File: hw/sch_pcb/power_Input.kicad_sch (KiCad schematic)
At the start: 34 parts, among them J1 USBC_USB4105-GF-A, U1 USBLC6-2SC6

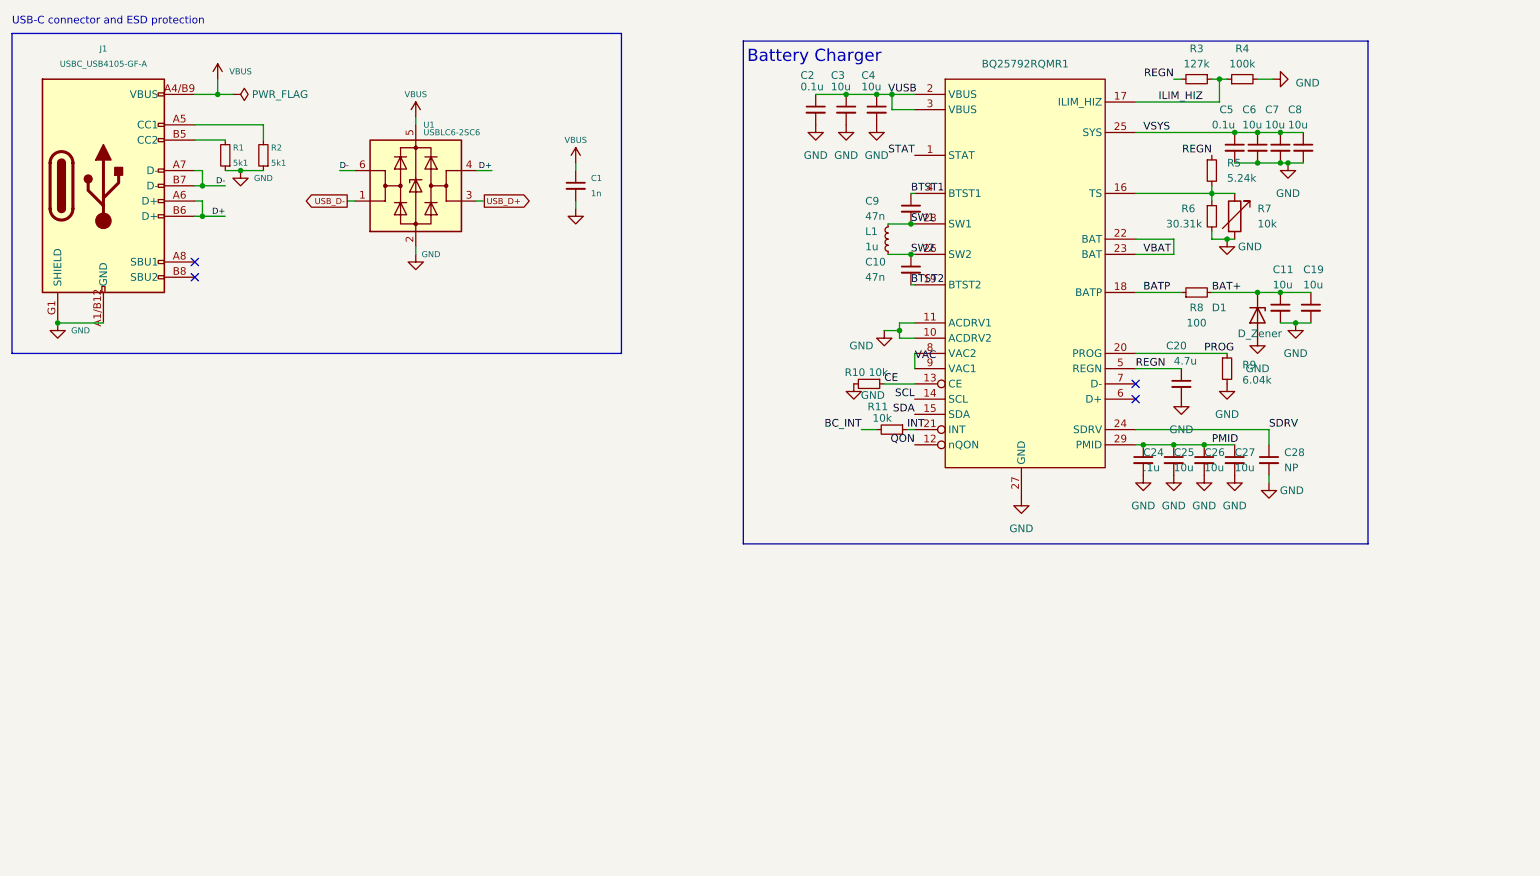
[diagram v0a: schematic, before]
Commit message: work of the schematics of charger completed.
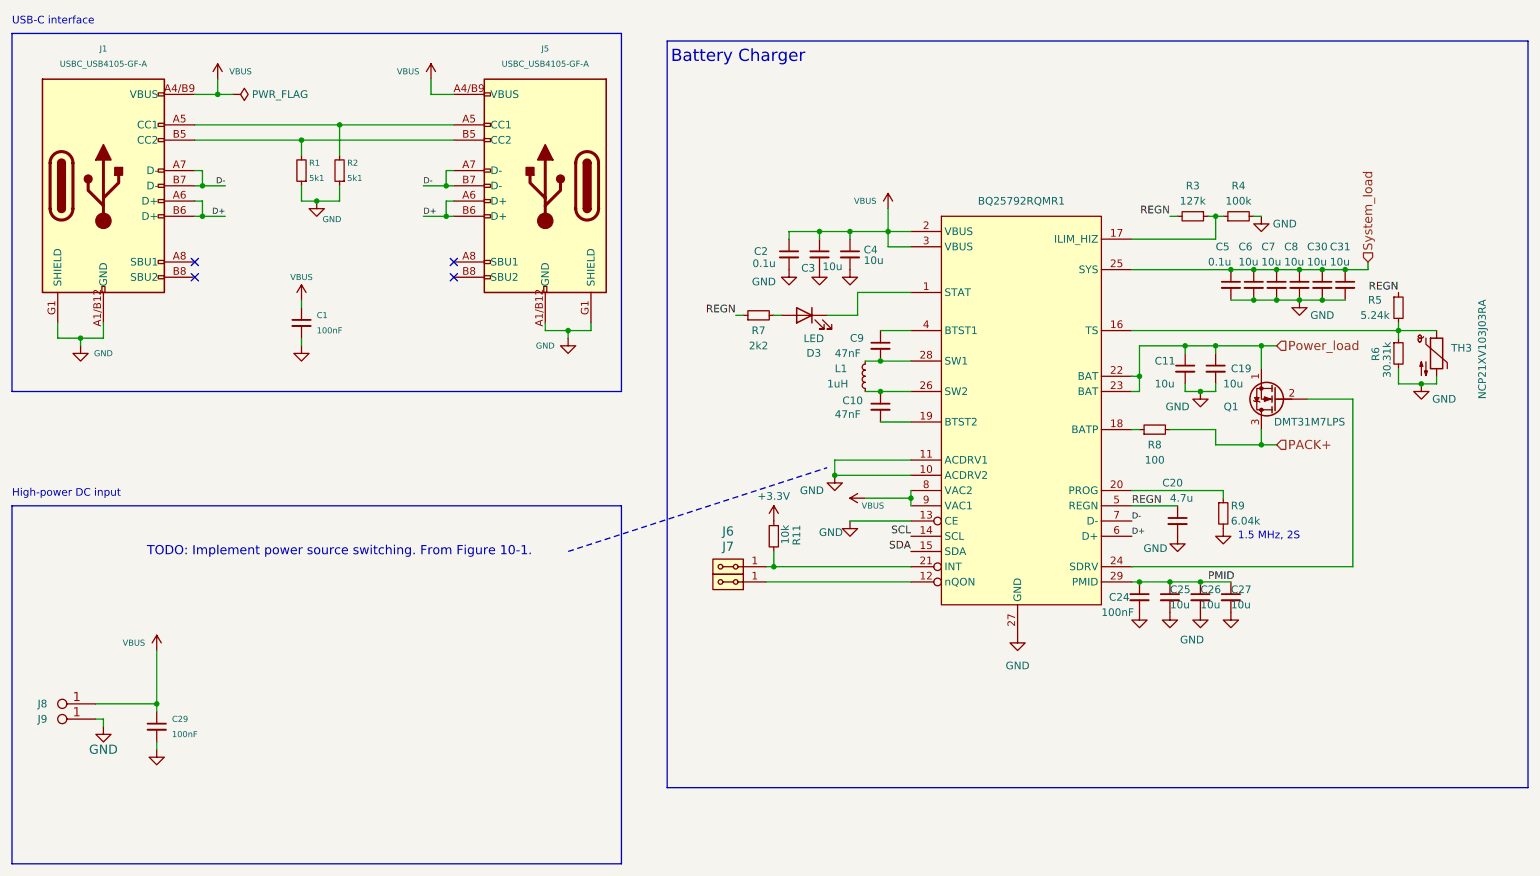
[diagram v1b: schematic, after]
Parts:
- removed C28: NP, Capacitor_SMD:C_0402_1005Metric, symbol Device:C_Small
- removed D1: D_Zener, Diode_SMD:D_SOD-323F, symbol Device:D_Zener
- removed R10: 10k, Resistor_SMD:R_0402_1005Metric, symbol Device:R_Small
- removed R7: 10k, Resistor_SMD:R_0402_1005Metric, symbol Device:R_Variable
- removed U1: USBLC6-2SC6, Package_TO_SOT_SMD:SOT-23-6, symbol Power_Protection:USBLC6-2SC6
- added C29: 100nF, Capacitor_SMD:C_0805_2012Metric, symbol Device:C_Small
- added C30, C31: 10u, Capacitor_SMD:C_0805_2012Metric, symbol Device:C_Small
- added D3: LED, symbol Device:LED
- added J5: USBC_USB4105-GF-A, Mlab_CON:USBC GCT_USB4105-GF-A, symbol MLAB_CONNECTORS:USBC_USB4105-GF-A
- added J6, J7: HEADER_2x01_PARALLEL, symbol MLAB_HEADER:HEADER_2x01_PARALLEL
- added J8, J9: CONN1_1, Mlab_Con:WAGO256, symbol LION2CELL01D-rescue:CONN1_1
- added Q1: DMT31M7LPS, Mlab_IO:PowerDI5060-8, symbol Device:Q_NMOS_SGD
- added R7: 2k2, Resistor_SMD:R_0805_2012Metric, symbol Device:R_Small
- added TH3: NCP21XV103J03RA, Resistor_SMD:R_0805_2012Metric, symbol Device:Thermistor_NTC
- C1: value 1n -> 100nF
- C10: value 47n -> 47nF; footprint Capacitor_SMD:C_0402_1005Metric -> Capacitor_SMD:C_0805_2012Metric
- C24: value .1u -> 100nF
- C9: value 47n -> 47nF
- L1: value 1u -> 1uH
- R8: footprint Resistor_SMD:R_0402_1005Metric -> Resistor_SMD:R_0805_2012Metric
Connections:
- net CE is gone; now on net GND: BQ25792RQMR1.13 (CE)
- net VAC is gone; now on net VBUS: BQ25792RQMR1.8 (VAC2), BQ25792RQMR1.9 (VAC1)
- net VBAT is gone; now on net Power_load: BQ25792RQMR1.22 (BAT), BQ25792RQMR1.23 (BAT)
- net VUSB is gone; now on net VBUS: BQ25792RQMR1.2 (VBUS), BQ25792RQMR1.3 (VBUS), C2.1, C3.1, C4.1
- net D+: now also BQ25792RQMR1.6 (D+), J5.A6 (D+), J5.B6 (D+)
- net D-: now also BQ25792RQMR1.7 (D-), J5.A7 (D-), J5.B7 (D-)
- net GND: now also C29.2, C30.2, C31.2, J5.A1/B12 (GND), J5.B1/A12 (GND), J5.G1 (SHIELD), J5.G2 (SHIELD), J5.G3 (SHIELD), J5.G4 (SHIELD), J9.1 (P1), TH3.2
- net REGN: now also R7.1
- net VBUS: now also C29.1, J5.A4/B9 (VBUS), J5.B4/A9 (VBUS), J8.1 (P1)
- net at BQ25792RQMR1.16 (TS), R5.2, R6.1: now also TH3.1
- net at J1.B5 (CC2), R1.2: now also J5.B5 (CC2)
- net at J1.A5 (CC1), R2.2: now also J5.A5 (CC1)
- net BAT+ renamed Power_load
- net Power_load: now also Q1.1 (S); no longer R8.2
- net BATP: no longer names the net of BQ25792RQMR1.18 (BATP), R8.1
- net BC_INT: no longer names the net of R11.2
- net BC_INT: now also BQ25792RQMR1.21 (INT), J6.1, J6.2
- net BTST1: no longer names the net of BQ25792RQMR1.4 (BTST1), C9.1
- net BTST2: no longer names the net of BQ25792RQMR1.19 (BTST2), C10.2
- net ILIM_HIZ: no longer names the net of BQ25792RQMR1.17 (ILIM_HIZ), R3.1, R4.1
- net INT renamed +3.3V
- net +3.3V: no longer BQ25792RQMR1.21 (INT)
- net PROG: no longer names the net of BQ25792RQMR1.20 (PROG), R9.1
- net QON: no longer names the net of BQ25792RQMR1.12 (nQON)
- net QON: now also J7.1, J7.2
- net SDRV: no longer names the net of BQ25792RQMR1.24 (SDRV)
- net SDRV: now also Q1.2 (G)
- net STAT: no longer names the net of BQ25792RQMR1.1 (STAT)
- net STAT: now also D3.1 (K)
- net SW1: no longer names the net of BQ25792RQMR1.28 (SW1), C9.2, L1.2
- net SW2: no longer names the net of BQ25792RQMR1.26 (SW2), C10.1, L1.1
- net VSYS renamed System_load
- net System_load: now also C30.1, C31.1
- new net: D3.2 (A), R7.2
- new net PACK+: Q1.3 (D), R8.2
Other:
- note added: "1.5 MHz, 2S"
- note added: "High-power DC input"
- note added: "TODO: Implement power source switching. From Figure 10-1."
- note added: "USB-C interface"
- note removed: "USB-C connector and ESD protection"
- moved on the sheet: BQ25792RQMR1, C1, C10, C11, C19, C2, C20, C24, C25, C26, C27, C3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

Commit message: Schematics work. PCB layout initial schematics import.
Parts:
- D3: footprint (none) -> Mlab_D:LED_1206
- J6, J7: footprint (none) -> Mlab_Pin_Headers:Straight_1x02
- J8, J9: footprint Mlab_Con:WAGO256 -> Mlab_CON:WAGO256
- U1: renamed from BQ25792RQMR1; value ~ -> BQ25792RQMR1; footprint Lipo_Charger:BQ25792 -> Mlab_IO:Texas_RQM0029A_VQFN-HR-28_4x4mm_P0.5mm
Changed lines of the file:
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@@
 			)
 		)
-		(property "Footprint" ""
+		(property "Footprint" "Mlab_D:LED_1206"
 			(at 157.48 76.2 0)
 			(effects
@@
 			)
 		)
-		(property "Footprint" "Mlab_Con:WAGO256"
+		(property "Footprint" "Mlab_CON:WAGO256"
 			(at 30.48 140.97 0)
 			(effects
@@
 			)
 		)
-		(property "Footprint" ""
+		(property "Footprint" "Mlab_Pin_Headers:Straight_1x02"
 			(at 144.78 118.11 0)
 			(effects
@@
 					(size 1.524 1.524)
 				)
+				(hide yes)
 			)
 		)
@@
 		(on_board yes)
 		(dnp no)
-		(fields_autoplaced yes)
-		(property "Reference" "BQ25792RQMR1"
-			(at 193.675 57.15 0)
+		(property "Reference" "U1"
+			(at 194.31 57.15 0)
 			(effects
 				(font
@@
 			)
 		)
-		(property "Value" "~"
-			(at 199.39 57.15 0)
+		(property "Value" "BQ25792RQMR1"
+			(at 194.31 88.9 90)
 			(effects
 				(font
@@
 			)
 		)
-		(property "Footprint" "Lipo_Charger:BQ25792"
+		(property "Footprint" "Mlab_IO:Texas_RQM0029A_VQFN-HR-28_4x4mm_P0.5mm"
 			(at 199.39 57.15 0)
 			(effects
@@
 			(project "LION2CELL02"
 				(path "/cf3ec207-cc3b-4c92-9c2d-71c8a9dee6d9/84542805-f3a9-4fad-892e-419f78d99400"
-					(reference "BQ25792RQMR1")
+					(reference "U1")
 					(unit 1)
 				)
@@
 			)
 		)
-		(property "Footprint" "Mlab_Con:WAGO256"
+		(property "Footprint" "Mlab_CON:WAGO256"
 			(at 30.48 138.43 0)
 			(effects
@@
 			)
 		)
-		(property "Footprint" ""
+		(property "Footprint" "Mlab_Pin_Headers:Straight_1x02"
 			(at 144.78 120.65 0)
 			(effects
@@
 					(size 1.524 1.524)
 				)
+				(hide yes)
 			)
 		)

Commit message: Layout WiP.
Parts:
- removed J5: USBC_USB4105-GF-A, Mlab_CON:USBC GCT_USB4105-GF-A, symbol MLAB_CONNECTORS:USBC_USB4105-GF-A
- C2, C20, C9: footprint Capacitor_SMD:C_0402_1005Metric -> Capacitor_SMD:C_0805_2012Metric
- C24, C5: footprint Capacitor_SMD:C_0402_1005Metric -> Capacitor_SMD:C_0603_1608Metric
- C25: footprint Capacitor_SMD:C_0603_1608Metric -> Capacitor_SMD:C_0805_2012Metric
- Q1: footprint Mlab_IO:PowerDI5060-8 -> Mlab_T:D_POWERDI5060-8_6.0x5.1mm_P1.27mm
- R11, R3, R4, R5, R6, R9: footprint Resistor_SMD:R_0402_1005Metric -> Resistor_SMD:R_0805_2012Metric
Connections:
- net PMID: no longer names the net of C24.1, C25.1, C26.1, C27.1, U1.29 (PMID)
- no-connect marks 4 -> 2

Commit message: Partially routed PCB.
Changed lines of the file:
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@@
-		)
-	)
-	(label "SDA"
-		(at 175.26 115.57 180)
-		(fields_autoplaced yes)
-		(effects
-			(font
-				(size 1.27 1.27)
-			)
-			(justify right bottom)
 		)
 	)
@@
 			)
 			(justify left bottom)
-		)
-	)
-	(label "SCL"
-		(at 175.26 113.03 180)
-		(fields_autoplaced yes)
-		(effects
-			(font
-				(size 1.27 1.27)
-			)
-			(justify right bottom)
 		)
 	)
@@
 			)
 			(justify left)
+		)
+	)
+	(hierarchical_label "SDA"
+		(shape input)
+		(at 175.26 115.57 180)
+		(fields_autoplaced yes)
+		(effects
+			(font
+				(size 1.524 1.524)
+			)
+			(justify right)
 		)
 	)
@@
 		)
 	)
+	(hierarchical_label "SCL"
+		(shape input)
+		(at 175.26 113.03 180)
+		(fields_autoplaced yes)
+		(effects
+			(font
+				(size 1.524 1.524)
+			)
+			(justify right)
+		)
+	)

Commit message: Syncing board with schematics. Roughly placing the switching regulator.
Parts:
- R9: value 6.04k -> 8k2
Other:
- note added: "750 kHz, 2S"
- note removed: "1.5 MHz, 2S"
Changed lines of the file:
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@@
 		)
 	)
-	(text "1.5 MHz, 2S"
-		(exclude_from_sim no)
-		(at 234.95 113.03 0)
+	(text "750 kHz, 2S"
+		(exclude_from_sim no)
+		(at 238.76 109.22 0)
 		(effects
 			(font
@@
 			)
 		)
-		(property "Value" "6.04k"
+		(property "Value" "8k2"
 			(at 228.6 110.49 0)
 			(effects
@@
 			(at 227.33 109.22 0)
 			(effects
+				(font
+					(size 1.27 1.27)
+				)
+				(hide yes)
+			)
+		)
+		(property "UST_ID" ""
+			(at 227.33 109.22 0)
+			(effects

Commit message: Routed switching regulator Starting of layout cleanup. Uniforming of charger and switching regulator inductors.
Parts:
- L1: value 1uH -> 2.2uH; footprint Inductor_SMD:L_1008_2520Metric -> Inductor_SMD:L_Vishay_IHLP-2020; UST_ID (none) -> 669e8efe6fdfe6f54e2eb7e6
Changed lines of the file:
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@@
 		)
 	)
+	(netclass_flag ""
+		(length 2.54)
+		(shape round)
+		(at 214.63 68.58 180)
+		(fields_autoplaced yes)
+		(effects
+			(font
+				(size 1.524 1.524)
+			)
+			(justify right bottom)
+		)
+		(property "Netclass" "HIGH_I"
+			(at 215.5952 71.12 0)
+			(effects
+				(font
+					(size 1.27 1.27)
+					(italic yes)
+				)
+				(justify left)
+			)
+		)
+	)
+	(netclass_flag ""
+		(length 2.54)
+		(shape round)
+		(at 59.69 39.37 180)
+		(fields_autoplaced yes)
+		(effects
+			(font
+				(size 1.524 1.524)
+			)
+			(justify right bottom)
+		)
+		(property "Netclass" "HIGH_I"
+			(at 60.6552 41.91 0)
+			(effects
+				(font
+					(size 1.27 1.27)
+					(italic yes)
+				)
+				(justify left)
+			)
+		)
+	)
 	(symbol
 		(lib_id "power:GND")
@@
 			)
 		)
-		(property "Value" "1uH"
+		(property "Value" "2.2uH"
 			(at 161.29 87.63 0)
 			(effects
@@
 			)
 		)
-		(property "Footprint" "Inductor_SMD:L_1008_2520Metric"
+		(property "Footprint" "Inductor_SMD:L_Vishay_IHLP-2020"
 			(at 167.64 86.36 0)
 			(effects
@@
 			(at 167.64 86.36 0)
 			(effects
+				(font
+					(size 1.27 1.27)
+				)
+				(hide yes)
+			)
+		)
+		(property "UST_ID" "669e8efe6fdfe6f54e2eb7e6"
+			(at 167.64 86.36 0)
+			(effects

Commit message: USB data lines layout improvement. Zones definitions for improving noise imunity.
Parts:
- J6, J7: footprint Mlab_Pin_Headers:Straight_1x02 -> Mlab_Pin_Headers:Straight_2x01
- Q1: value DMT31M7LPS -> DMTH3002LPS; Manufacturer_Part_Number DMT31M7LPS-13 -> (none)
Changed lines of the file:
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@@
 			)
 		)
-		(property "Value" "DMT31M7LPS"
+		(property "Value" "DMTH3002LPS"
 			(at 247.65 93.98 0)
 			(effects
@@
 			)
 		)
-		(property "Datasheet" "https://eu.mouser.com/datasheet/2/115/DIOD_S_A0006645066_1-2542967.pdf"
+		(property "Datasheet" "https://eu.mouser.com/datasheet/2/115/DIOD_S_A0003132884_1-2542222.pdf"
 			(at 236.22 90.17 0)
 			(effects
@@
 			)
 		)
-		(property "Manufacturer_Part_Number" " DMT31M7LPS-13"
-			(at 236.22 90.17 0)
-			(effects
-				(font
-					(size 1.27 1.27)
-				)
-				(hide yes)
-			)
-		)
 		(property "UST_ID" "669990696fdfe6f54e2eb28a"
 			(at 236.22 90.17 0)
@@
 			)
 		)
-		(property "Footprint" "Mlab_Pin_Headers:Straight_1x02"
+		(property "Footprint" "Mlab_Pin_Headers:Straight_2x01"
 			(at 144.78 118.11 0)
 			(effects
@@
 			)
 		)
-		(property "Datasheet" "~"
+		(property "Datasheet" "https://www.vishay.com/docs/34563/ihlp-2020cz-8a.pdf"
 			(at 167.64 86.36 0)
 			(effects
@@
 			)
 		)
-		(property "Footprint" "Mlab_Pin_Headers:Straight_1x02"
+		(property "Footprint" "Mlab_Pin_Headers:Straight_2x01"
 			(at 144.78 120.65 0)
 			(effects
